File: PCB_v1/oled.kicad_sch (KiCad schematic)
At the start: 15 parts, among them J7 Conn_02x04_Odd_Even, SW1 SW_Push, SW2 SW_Push, SW3 SW_Push, SW4 SW_Push, SW5 SW_Push, SW6 SW_Push

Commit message: PCB changes before changing Seth's clock
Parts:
- removed C1, C14, C2, C3, C4, C5: .1uF, Capacitor_SMD:C_0805_2012Metric, symbol Device:C
- removed RN1: 10k, Resistor_THT:R_Array_SIP7, symbol Device:R_Network06_Split
- removed RN2: 1K, Resistor_THT:R_Array_SIP12, symbol Device:R_Pack06_SIP_Split
- added C1, C2: CA0612KRX7R7BB104, CAP_CA0612_3P2X1P6_YAG, symbol GT_LIbrary:CA0612KRX7R7BB104
- added RN1, RN2: 10k, symbol Device:R_Pack08_Split
- added RN3, RN4: 1k, symbol Device:R_Pack08_Split
- added TP1, TP2, TP3, TP4: TestPoint, symbol Connector:TestPoint
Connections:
- net 3V3: now also RN1.16 (R1.2), RN2.11 (R6.2), RN2.12 (R5.2), RN2.13 (R4.2), RN2.14 (R3.2), RN2.15 (R2.2), RN2.9 (R8.2)
- net Button1: now also C1.8, RN1.1 (R1.1), RN3.1 (R1.1)
- net Button2: now also C1.7, RN2.2 (R2.1), RN4.2 (R2.1)
- net Button3: now also C1.6, RN2.3 (R3.1), RN4.3 (R3.1)
- net Button4: now also C1.5, RN2.4 (R4.1), RN4.4 (R4.1)
- net Button5: now also C2.8, RN2.5 (R5.1), RN4.5 (R5.1)
- net Button6: now also C2.2, RN2.6 (R6.1), RN4.6 (R6.1)
- net GND: now also C1.1, C1.2, C1.3, C1.4, C2.1, C2.5, C2.6, C2.7
- net at SW4.2: now also RN4.13 (R4.2)
- net at SW1.2: now also RN3.16 (R1.2)
- net at SW2.2: now also RN4.15 (R2.2)
- net at SW6.2: now also RN4.11 (R6.2)
- net at SW5.2: now also RN4.12 (R5.2)
- net at SW3.2: now also RN4.14 (R3.2)
- new net: C2.3, RN2.7 (R7.1), RN4.7 (R7.1)
- new net: C2.4, RN2.8 (R8.1), RN4.8 (R8.1)

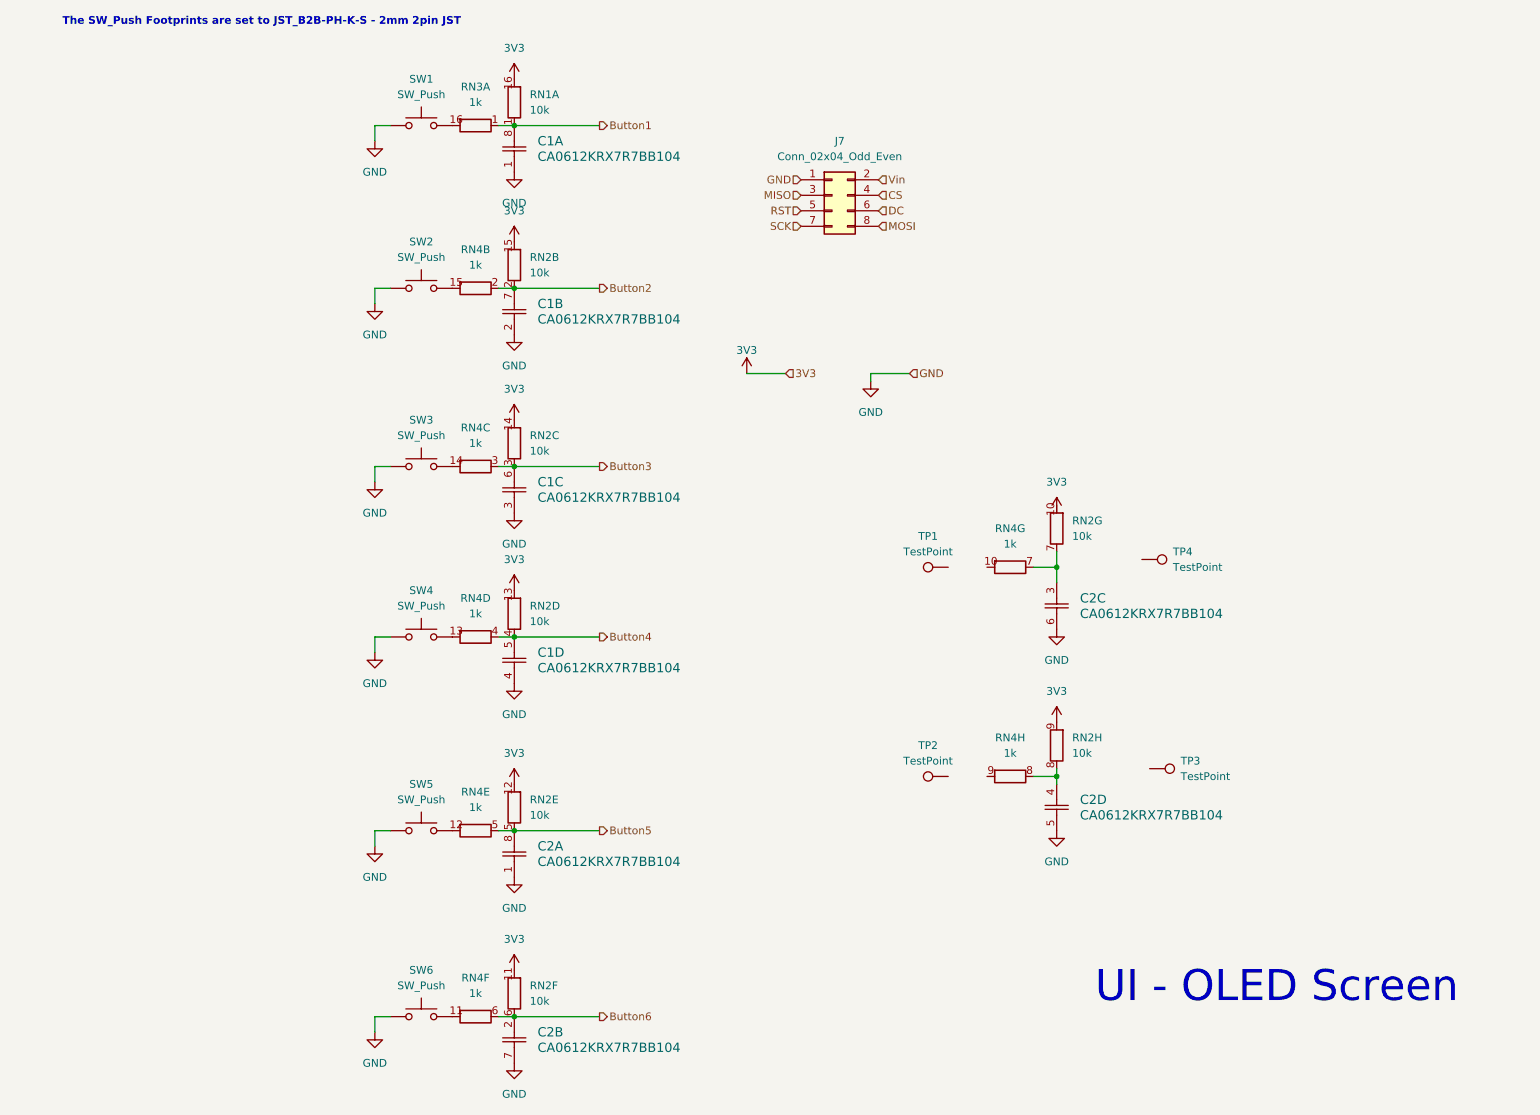
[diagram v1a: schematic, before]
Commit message: Update before adding AGND for the power delivery
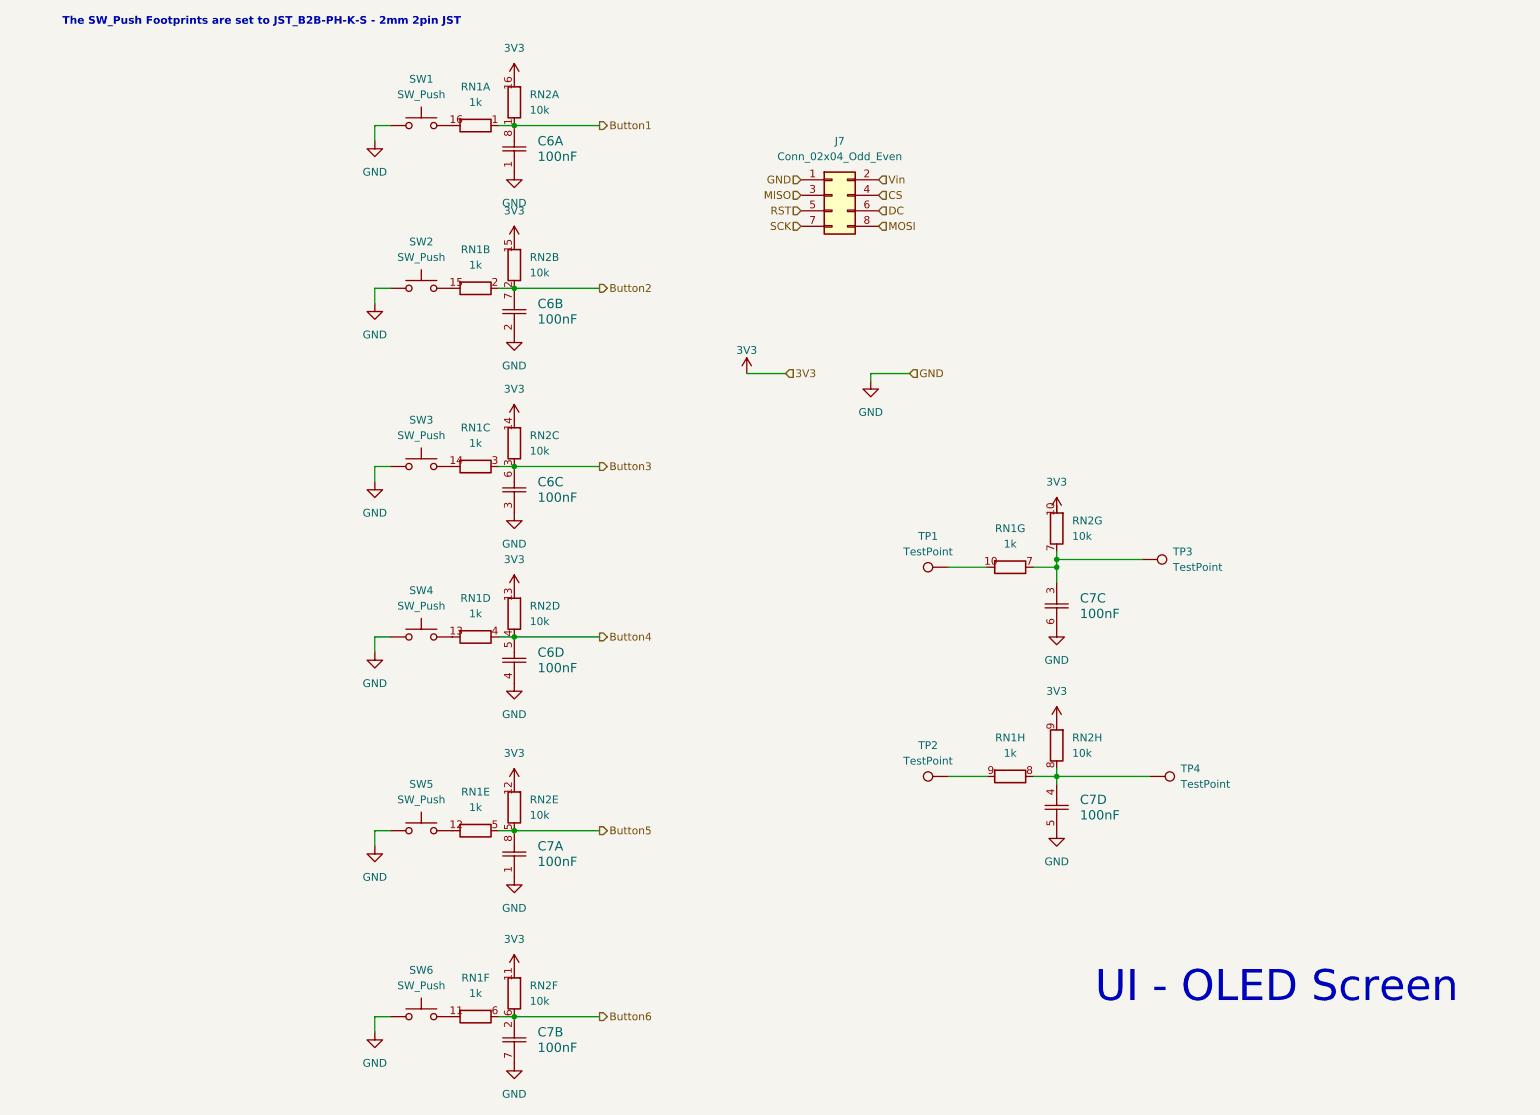
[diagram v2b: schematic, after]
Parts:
- C6: renamed from C1; value CA0612KRX7R7BB104 -> 100nF
- C7: renamed from C2; value CA0612KRX7R7BB104 -> 100nF
- SW2, SW3, SW4, SW5, SW6: footprint D&KD6R:D6R_CNK -> JST_B2B-PH-K-S
- TP1, TP2: footprint (none) -> TestPoint:TestPoint_THTPad_D1.0mm_Drill0.5mm
- TP3: renamed from TP4; footprint (none) -> TestPoint:TestPoint_THTPad_D1.0mm_Drill0.5mm
- TP4: renamed from TP3; footprint (none) -> TestPoint:TestPoint_THTPad_D1.0mm_Drill0.5mm
- renumbered RN4 to RN1, RN3 to RN1, RN1 to RN2
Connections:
- net at TP4.1: now also C7.4, RN1.8 (R8.1), RN2.8 (R8.1)
- net at C7.3, RN1.7 (R7.1), RN2.7 (R7.1): now also TP3.1
- net at TP2.1: now also RN1.9 (R8.2)
- net at TP1.1: now also RN1.10 (R7.2)
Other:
- moved on the sheet: TP4

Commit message: Initial placement draft
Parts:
- RN1: footprint (none) -> Parts_Library:RESCAXE50P280X160X55-16N; MFP (none) -> EXB-2HV102JV
- RN2: footprint (none) -> Parts_Library:RESCAXE50P280X160X55-16N
- renumbered SW1 to SW2, SW2 to SW3, SW3 to SW4, SW4 to SW5, SW5 to SW6, SW6 to SW7, TP1 to TP3, TP2 to TP4, TP3 to TP5, TP4 to TP6
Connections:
- net 3V3: now also RN2.10 (R7.2)
- net Button1: now also RN2.8 (R8.1); no longer RN2.1 (R1.1)
- net Button2: now also RN2.7 (R7.1); no longer RN2.2 (R2.1)
- net Button3: now also RN2.6 (R6.1); no longer RN2.3 (R3.1)
- net Button4: now also RN2.5 (R5.1); no longer RN2.4 (R4.1)
- net Button5: now also C7.4, RN2.4 (R4.1); no longer C7.8, RN2.5 (R5.1)
- net Button6: now also C7.3, RN2.3 (R3.1); no longer C7.2, RN2.6 (R6.1)
- net GND: now also C7.8; no longer C7.1
- net at RN1.8 (R8.1), TP6.1: now also C7.1, RN2.1 (R1.1); no longer C7.4, RN2.8 (R8.1)
- net at RN1.7 (R7.1), TP5.1: now also C7.2, RN2.2 (R2.1); no longer C7.3, RN2.7 (R7.1)

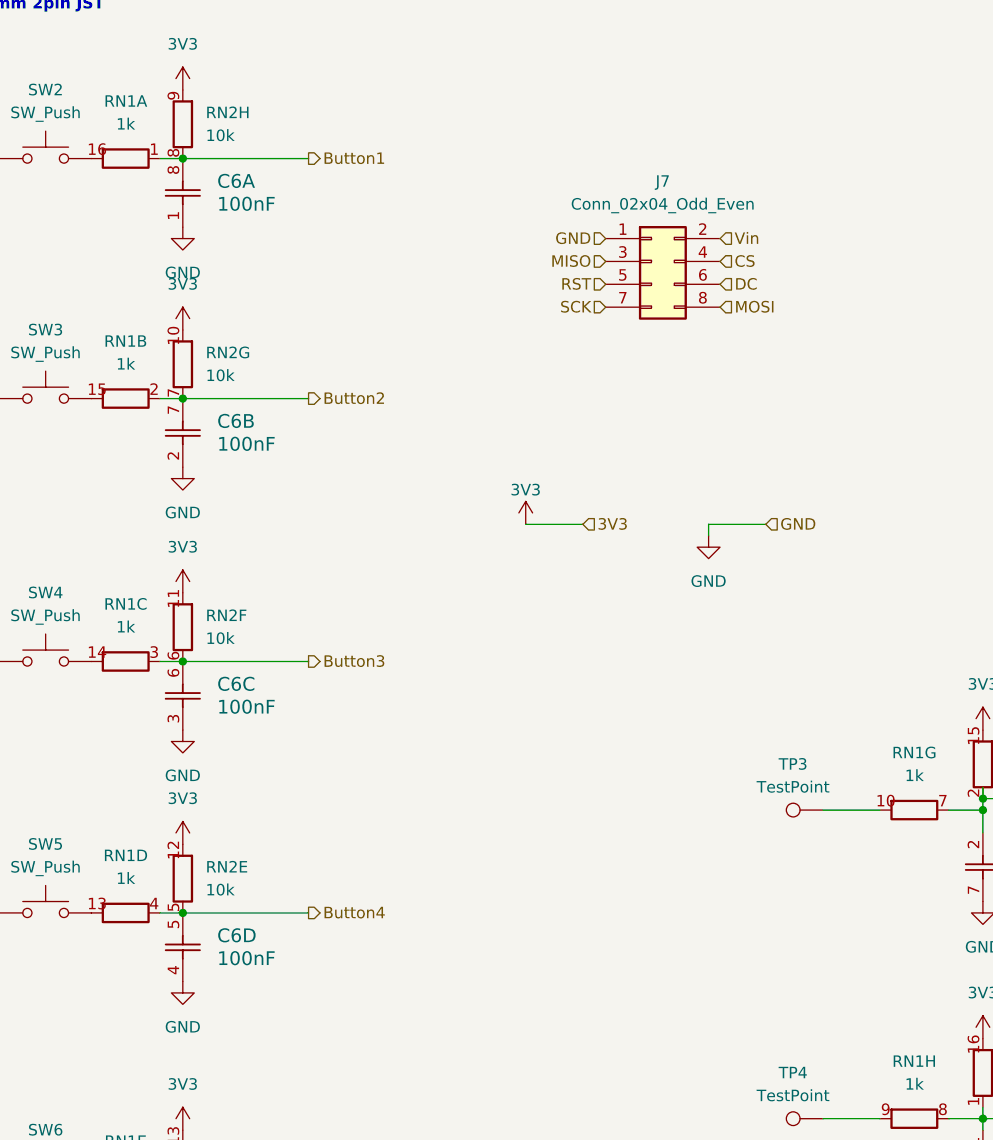
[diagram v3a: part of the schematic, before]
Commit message: adjusted placments
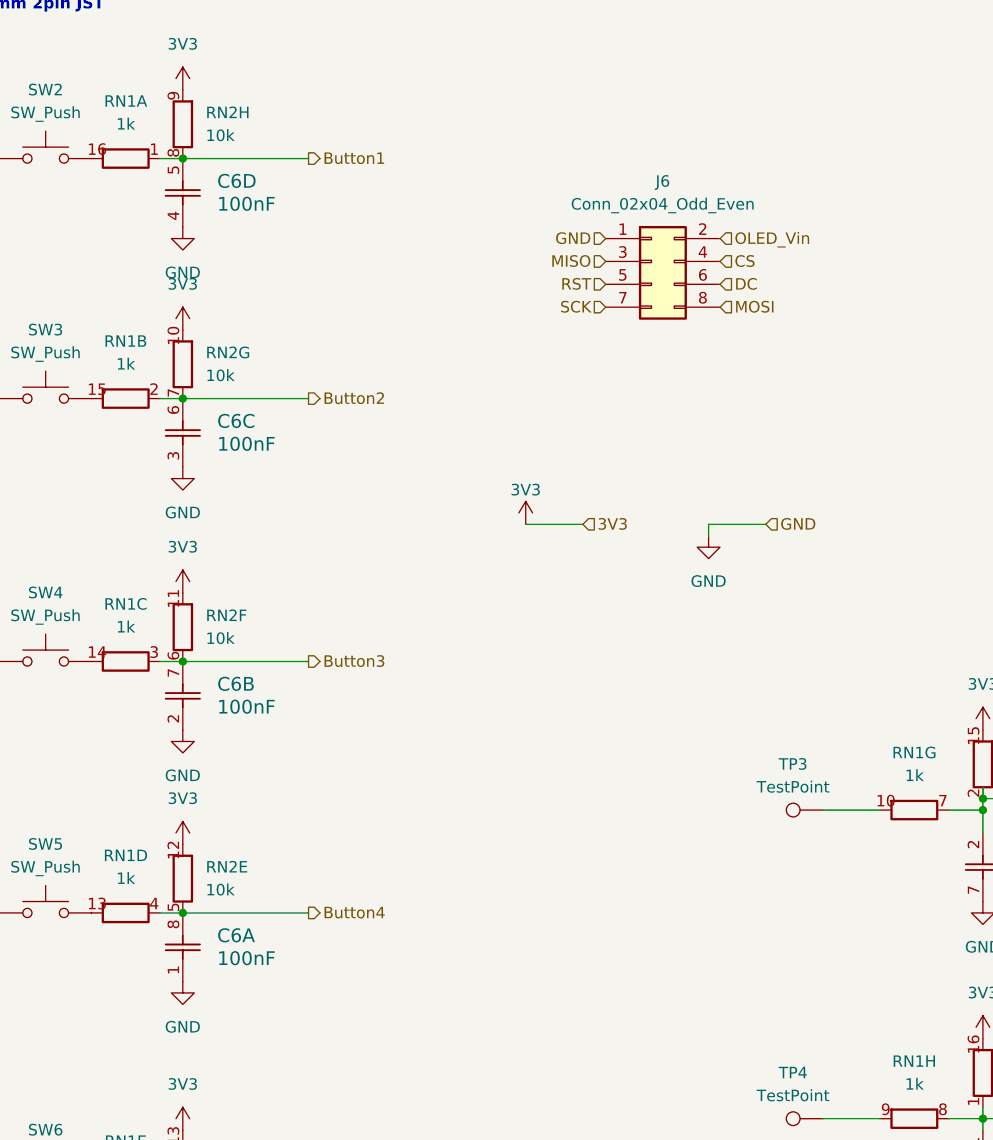
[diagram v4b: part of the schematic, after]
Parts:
- renumbered J7 to J6
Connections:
- net Button1: now also C6.5; no longer C6.8
- net Button2: now also C6.6; no longer C6.7
- net Button3: now also C6.7; no longer C6.6
- net Button4: now also C6.8; no longer C6.5
- net Vin renamed OLED_Vin

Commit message: Power Layout done
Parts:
- added U7, U8: SMS05T1G, SOIC_05T1G_ONS, symbol GT_LIbrary:SMS05T1G
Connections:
- net GND: now also U7.2, U7.5, U8.2, U8.5
- net B4: now reaches RN1.13 (R4.2), SW5.2
- net B4: now also U7.6
- net B1: now reaches RN1.16 (R1.2), SW2.2
- net B1: now also U7.4
- net B2: now reaches RN1.15 (R2.2), SW3.2
- net B2: now also U7.3
- net B8: now reaches C7.1, RN1.8 (R8.1), RN2.1 (R1.1), TP6.1
- net B8: now also U8.1
- net B5: now reaches RN1.12 (R5.2), SW6.2
- net B5: now also U8.4
- net B6: now reaches RN1.11 (R6.2), SW7.2
- net B6: now also U8.3
- net B3: now reaches RN1.14 (R3.2), SW4.2
- net B3: now also U7.1
- net B7: now reaches C7.2, RN1.7 (R7.1), RN2.2 (R2.1), TP5.1
- net B7: now also U8.6
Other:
- moved on the sheet: SW2, SW3, SW4, SW5, SW6, SW7

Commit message: before annonation reset
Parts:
- SW2, SW3, SW4, SW5, SW6, SW7: MFP (none) -> JST_B2B-PH-K-S
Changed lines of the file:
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@@
 			)
 		)
-		(property "Datasheet" "~"
+		(property "Datasheet" "JST_B2B-PH-K-S"
 			(at 72.39 111.76 0)
 			(effects
@@
 			)
 		)
-		(property "MFP" ""
+		(property "MFP" "JST_B2B-PH-K-S"
 			(at 72.39 116.84 0)
 			(effects
@@
 			)
 		)
-		(property "Datasheet" "~"
+		(property "Datasheet" "JST_B2B-PH-K-S"
 			(at 72.39 27.94 0)
 			(effects
@@
 			)
 		)
-		(property "MFP" ""
+		(property "MFP" "JST_B2B-PH-K-S"
 			(at 72.39 33.02 0)
 			(effects
@@
 			)
 		)
-		(property "Datasheet" "~"
+		(property "Datasheet" "JST_B2B-PH-K-S"
 			(at 72.39 54.61 0)
 			(effects
@@
 			)
 		)
-		(property "MFP" ""
+		(property "MFP" "JST_B2B-PH-K-S"
 			(at 72.39 59.69 0)
 			(effects
@@
 			)
 		)
-		(property "Datasheet" "~"
+		(property "Datasheet" "JST_B2B-PH-K-S"
 			(at 72.39 143.51 0)
 			(effects
@@
 			)
 		)
-		(property "MFP" ""
+		(property "MFP" "JST_B2B-PH-K-S"
 			(at 72.39 148.59 0)
 			(effects
@@
 			)
 		)
-		(property "Datasheet" "~"
+		(property "Datasheet" "JST_B2B-PH-K-S"
 			(at 72.39 83.82 0)
 			(effects
@@
 			)
 		)
-		(property "MFP" ""
+		(property "MFP" "JST_B2B-PH-K-S"
 			(at 72.39 88.9 0)
 			(effects
@@
 			)
 		)
-		(property "Datasheet" "~"
+		(property "Datasheet" "JST_B2B-PH-K-S"
 			(at 72.39 173.99 0)
 			(effects
@@
 			)
 		)
-		(property "MFP" ""
+		(property "MFP" "JST_B2B-PH-K-S"
 			(at 72.39 179.07 0)
 			(effects
